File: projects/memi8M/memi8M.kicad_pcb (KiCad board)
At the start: 2 copper layers, 38 parts, among them J1 Conn_01x06, J2 Conn_01x02, J3 Conn_01x03, J4 Conn_01x06, SW1 SW_DIP_x05, U1 74HC595N, U10 74LS166N, U11 SST39VF1681_1682, U12 74LVC4245, U2 74HC595N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

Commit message: memi8M pcb update
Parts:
- moved J1 86.6 mm to (163.8, 40.6)
- moved U11 8.89 mm to (83.8, 99.1)
- moved SW1 5.24 mm to (200.7, 113.0)
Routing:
- net /SI_OE_A: track 0.00 -> 90.9 mm, vias 0 -> 3
- net /SI_RCLK: track 0.00 -> 82.7 mm, vias 0 -> 3
- net /SI_SRCLR: track 0.00 -> 81.0 mm, vias 0 -> 1
- net /SI_SER: track 0.00 -> 74.6 mm
- net /SI_SRCLK: track 0.00 -> 72.1 mm, vias 0 -> 3
- net /A1_3V: track 0.00 -> 55.8 mm, vias 0 -> 2
- net /FLASH_CE: track 0.00 -> 41.6 mm, vias 0 -> 1
- net /FLASH_OE: track 0.00 -> 36.7 mm, vias 0 -> 1
- net /A0_3V: track 0.00 -> 35.1 mm, vias 0 -> 2
- net /A17_3V: track 0.00 -> 27.7 mm
- net /D2_3V: track 0.00 -> 27.2 mm
- net /D6_3V: track 0.00 -> 27.2 mm
- net /D7_3V: track 0.00 -> 25.2 mm
- net /D4_3V: track 0.00 -> 24.7 mm
- net /D0_3V: track 0.00 -> 24.7 mm
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
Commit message: memi8M pcb update vol. 2
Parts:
- moved C13 179.2 mm to (92.7, 111.8)
- moved C9 171.9 mm to (97.8, 74.9), turned to 90 degrees
- moved C3 167.8 mm to (102.9, 39.4), turned to 270 degrees
- moved C4 163.8 mm to (106.7, 39.4), turned to 270 degrees
- moved C7 157.9 mm to (142.2, 119.4)
- moved C12 152.3 mm to (125.7, 115.6), turned to 270 degrees
- moved C10 150.6 mm to (118.1, 74.9), turned to 90 degrees
- moved C5 146.1 mm to (124.5, 39.4), turned to 270 degrees
- moved C11 126.9 mm to (141.0, 74.9), turned to 90 degrees
- moved C6 116.6 mm to (163.8, 99.1), turned to 180 degrees
- moved C8 106.5 mm to (181.6, 92.7)
- moved C2 95.6 mm to (176.5, 43.2), turned to 90 degrees
- moved C1 89.4 mm to (188.0, 53.3), turned to 90 degrees
- moved D1 82.4 mm to (182.9, 53.3), turned to 180 degrees
- moved R1 80.1 mm to (179.1, 55.9), turned to 270 degrees
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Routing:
- net GND_: track 0.00 -> 140.7 mm, vias 0 -> 5
- net VCC_: track 0.00 -> 138.7 mm, vias 0 -> 3
- net /DATA_OE: track 0.00 -> 124.5 mm, vias 0 -> 1
- net /SI_OE_D: track 0.00 -> 116.2 mm, vias 0 -> 2
- net /DATA_DIR: track 0.00 -> 115.3 mm, vias 0 -> 1
- net Net-(U3-Pad9): track 0.00 -> 102.7 mm, vias 0 -> 2
- net /SI_SRCLR: track 81.0 -> 171.5 mm, vias 1 -> 2
- net /SI_RCLK: track 82.7 -> 173.2 mm, vias 3 -> 4
- net /SI_SRCLK: track 72.1 -> 160.9 mm, vias 3 -> 4
- net /SO_CLR: track 0.00 -> 43.1 mm, vias 0 -> 2
- net /SO_QH: track 0.00 -> 38.3 mm, vias 0 -> 1
- net /SI_OE_A: track 90.9 -> 122.0 mm, vias 3 -> 4
- net /ROM_OE: track 89.0 -> 119.2 mm
- net /SO_SHLD: track 0.00 -> 24.8 mm, vias 0 -> 1
- net /SO_CLK: track 0.00 -> 18.6 mm, vias 0 -> 1
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
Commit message: memi8M pcb update vol. 3
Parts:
- moved C1 6.48 mm to (181.6, 52.1), turned to 0 degrees
- moved C7 5.08 mm to (142.2, 114.3)
- moved U12 3.81 mm to (134.6, 105.4)
- moved J3 2.54 mm to (141.0, 92.7)
- moved D1 2.54 mm to (182.9, 55.9)
- moved R1 1.27 mm to (179.1, 57.1)
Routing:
- net GND_: track 140.7 -> 335.4 mm, vias 5 -> 16
- net VCC_: track 138.7 -> 256.4 mm, vias 3 -> 8
- net /DATA_DIR: track 115.3 -> 125.7 mm
- net /SO_CLR: track 43.1 -> 52.6 mm, vias 2 -> 1
- net /ROM_OE: track 119.2 -> 113.4 mm
- net /ROM_CE: track 70.1 -> 64.3 mm
- net /SO_QH: track 38.3 -> 43.0 mm
- net /D1_5V: track 91.3 -> 88.3 mm, vias 4 -> 6
- net /DATA_OE: track 124.5 -> 127.1 mm
- net /WE_5V: track 36.9 -> 34.4 mm
- net /D2_5V: track 92.0 -> 89.8 mm, vias 4 -> 6
- net /D0_5V: track 120.8 -> 118.7 mm
- net /SO_CLK: track 18.6 -> 20.4 mm
- net /D3_5V: track 66.7 -> 68.3 mm, vias 3 -> 4
- net /D3_3V: track 14.0 -> 15.6 mm
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
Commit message: memi8M pcb update vol. 4
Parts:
- moved C9 8.98 mm to (99.1, 66.0), turned to 0 degrees
- moved C12 3.81 mm to (129.5, 115.6), turned to 180 degrees
- turned C10 to 270 degrees
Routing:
- net GND_: track 335.4 -> 465.3 mm, vias 16 -> 17
- net +3V3_: track 13.1 -> 20.5 mm

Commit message: memi8M pcb update vol. 5 - all connections done
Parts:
- moved C9 7.73 mm to (97.8, 73.7), turned to 270 degrees
- moved C11 2.84 mm to (138.4, 73.7), turned to 270 degrees
- moved C13 2.54 mm to (90.2, 111.8)
- moved C10 1.27 mm to (118.1, 73.7)
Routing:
- net +3V3_: track 20.5 -> 346.0 mm, vias 0 -> 11
- net GND_: track 465.3 -> 622.0 mm, vias 17 -> 21
- net /DATA_OE: track 127.1 -> 129.2 mm
- net /D0_5V: track 118.7 -> 120.8 mm
- net /DATA_DIR: track 125.7 -> 127.8 mm
- net VCC_: track 256.4 -> 258.5 mm
- net /A1_3V: vias 2 -> 1
- net /A0_3V: vias 2 -> 1

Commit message: memi8M pcb update vol. 6 - pcb filled with copper
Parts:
- moved C3 14.0 mm to (88.9, 39.4)
- moved J1 3.81 mm to (163.8, 33.0)
- moved C10 1.27 mm to (118.1, 74.9)
- moved C9 1.27 mm to (97.8, 74.9)
- moved C6 1.27 mm to (165.1, 99.1)
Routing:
- net GND_: track 622.0 -> 1150.5 mm, vias 21 -> 99
- net +3V3_: track 346.0 -> 358.2 mm, vias 11 -> 17
- net VCC_: track 258.5 -> 269.9 mm, vias 8 -> 10
- net /SI_SRCLK: track 160.9 -> 166.3 mm
- net /SI_SRCLR: track 171.5 -> 175.8 mm
- net /SI_RCLK: track 173.2 -> 177.5 mm
- net /SI_OE_A: track 122.0 -> 126.3 mm
- net /D0_5V: track 120.8 -> 116.8 mm
- net /DATA_DIR: track 127.8 -> 123.8 mm
- net /SI_OE_D: track 116.2 -> 120.0 mm
- net /DATA_OE: track 129.2 -> 125.9 mm
- net /A0_5V: track 110.5 -> 112.6 mm
- net Net-(U3-Pad9): track 102.7 -> 104.8 mm
- net /SI_SER: track 73.0 -> 71.4 mm
- net /A16_5V: track 109.8 -> 111.3 mm
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- added copper zone on B.Cu, net GND_
- added copper zone on F.Cu, net GND_
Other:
- board outline added: 128.6 x 96.2 mm
- board text added: "memi8M SFCRevival®"

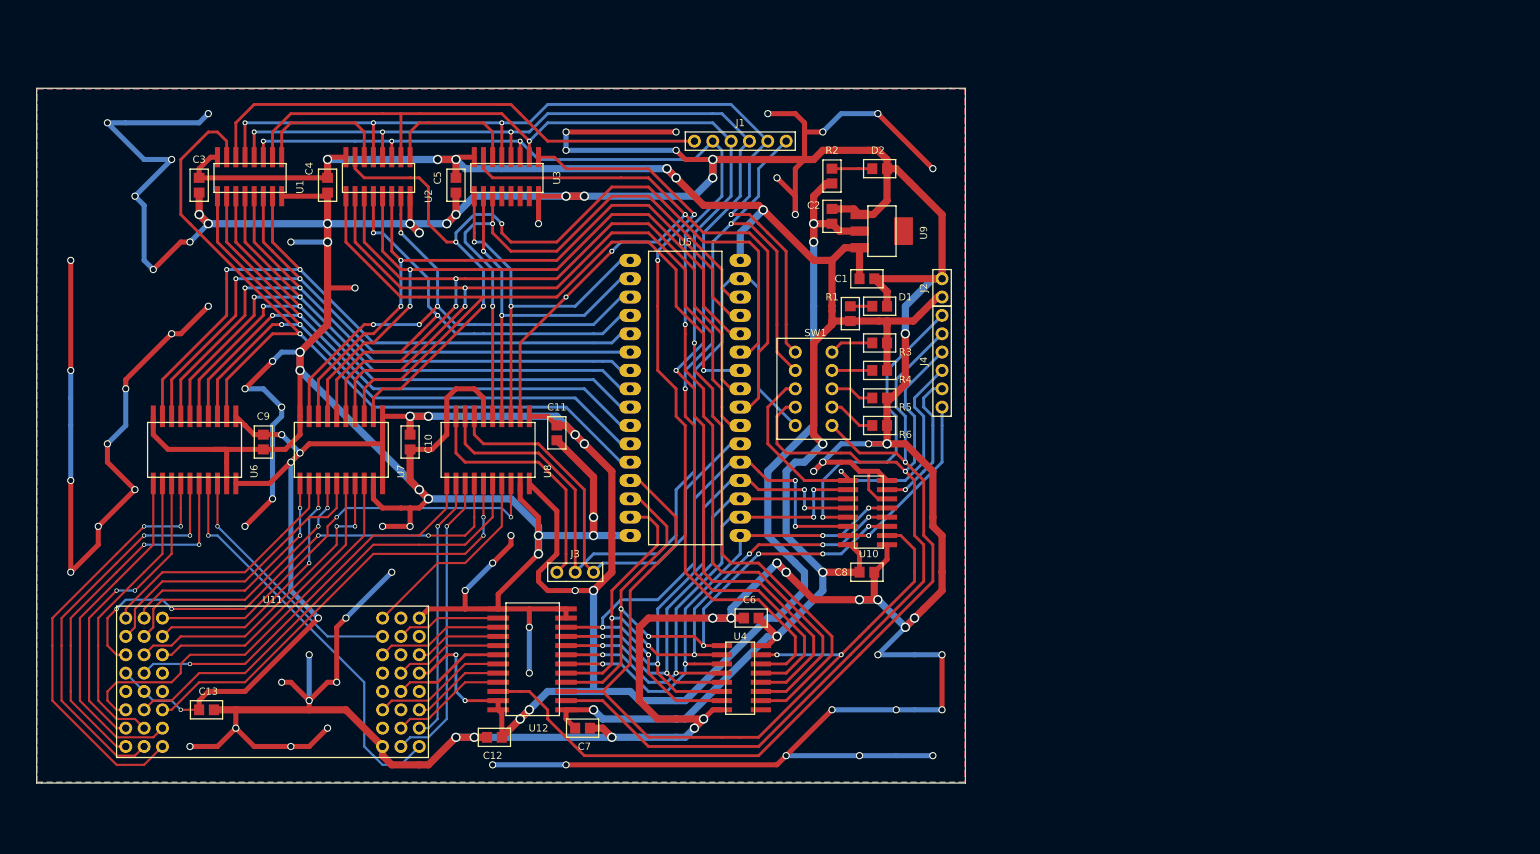
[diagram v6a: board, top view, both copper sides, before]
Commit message: Added mount holes.
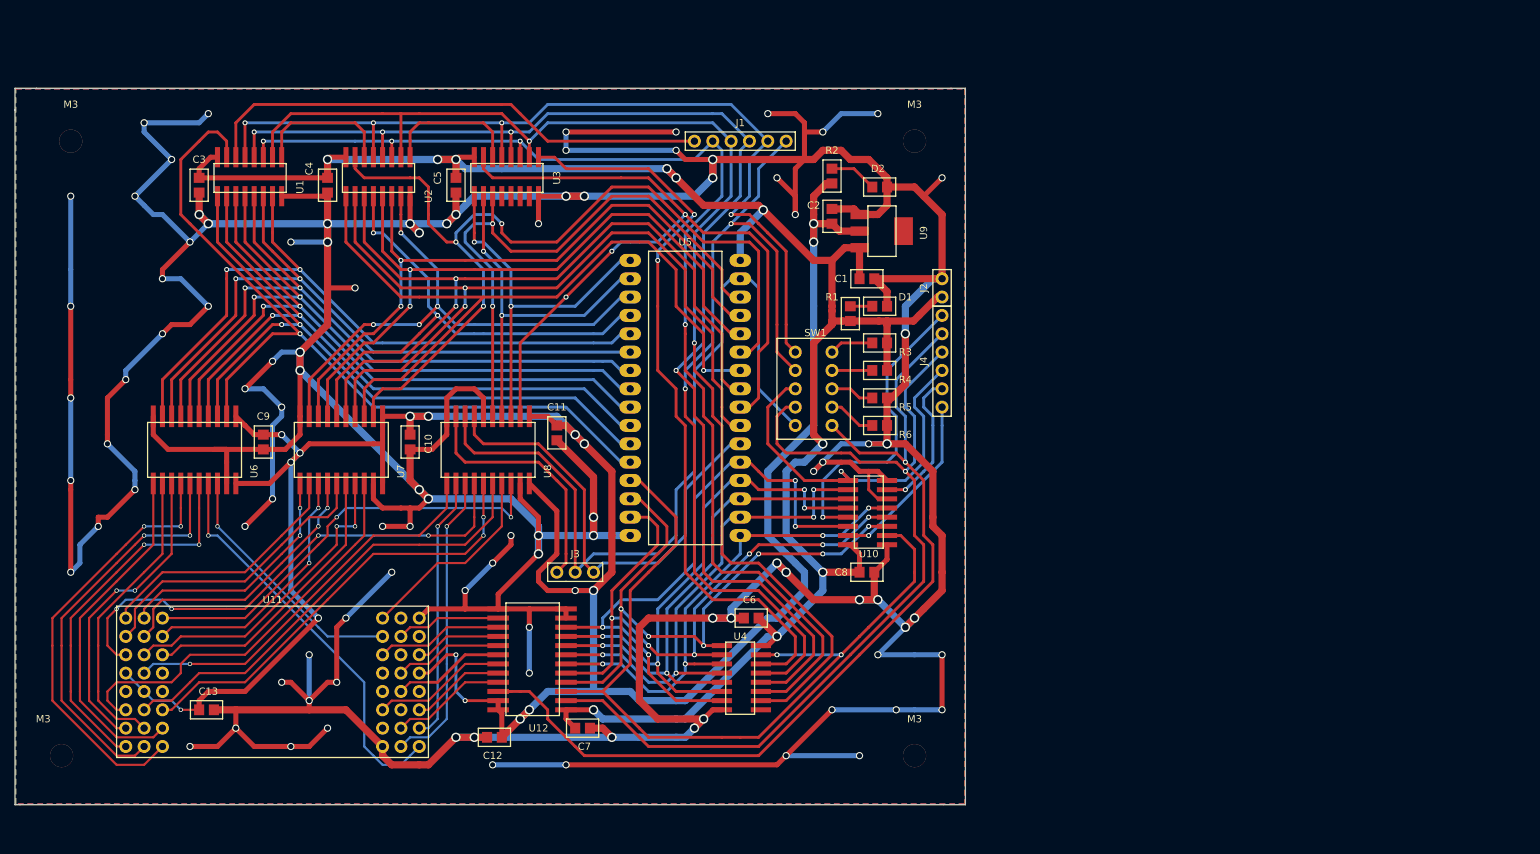
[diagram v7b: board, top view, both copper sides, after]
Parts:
- added M3: MOUNTHOLE_M3, alf64_mods:MOUNTHOLE_M3, F.Cu at (71.1, 33.0)
- added M3: MOUNTHOLE_M3, alf64_mods:MOUNTHOLE_M3, F.Cu at (69.8, 118.1)
- added M3: MOUNTHOLE_M3, alf64_mods:MOUNTHOLE_M3, F.Cu at (188.0, 33.0)
- added M3: MOUNTHOLE_M3, alf64_mods:MOUNTHOLE_M3, F.Cu at (188.0, 118.1)
- moved D2 2.54 mm to (182.9, 39.4)
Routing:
- net GND_: track 1150.5 -> 1138.9 mm
- net Net-(D2-Pad2): track 5.58 -> 6.63 mm
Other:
- board size 128.6 x 96.2 mm -> 131.6 x 99.2 mm

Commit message: memi8M pcb update vol. 7 - ready for gerber creation
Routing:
- net GND_: track 1138.9 -> 1287.4 mm, vias 99 -> 117
